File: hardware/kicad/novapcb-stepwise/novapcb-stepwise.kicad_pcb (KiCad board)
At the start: 6 copper layers, 90 x 70 mm, 129 parts, among them J1 USB-C_2.0, J10 CRSF_solder_pad, J11 ESC_solder_pad, J12 ESC_solder_pad, J13 ESC_solder_pad, J14 ESC_solder_pad, J15 ESC_solder_pad, J16 ESC_solder_pad, J17 ESC_solder_pad, J18 ESC_solder_pad, J19 MAUCH2_6P, J2 microSD_DM3AT, J20 CAN_4P, J3 TELEM_6P, J4 MAUCH_6P, J5 GPS_MAG_10P, J9 SWD_10P, Q2 AO3401A, Q3 AO4262E, Q4 AO4262E, Q5 AO3400A, U1 STM32H743VITx, U11 LM74700-Q1, U12 LM74700-Q1, U13 LP5907MFX-3.3, U14 TJA1051TK/3, U15 PESD2CAN, U2 AP2112K-3.3, U3 ICM-42688-P_LGA-14_2.5x3mm_P0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, U4 DPS310, U5 USBLC6-2P6, U6 TPS25940A, U7 LPS22HB, U8 BMI088, U9 LSM6DSV16X, Y1 8MHz

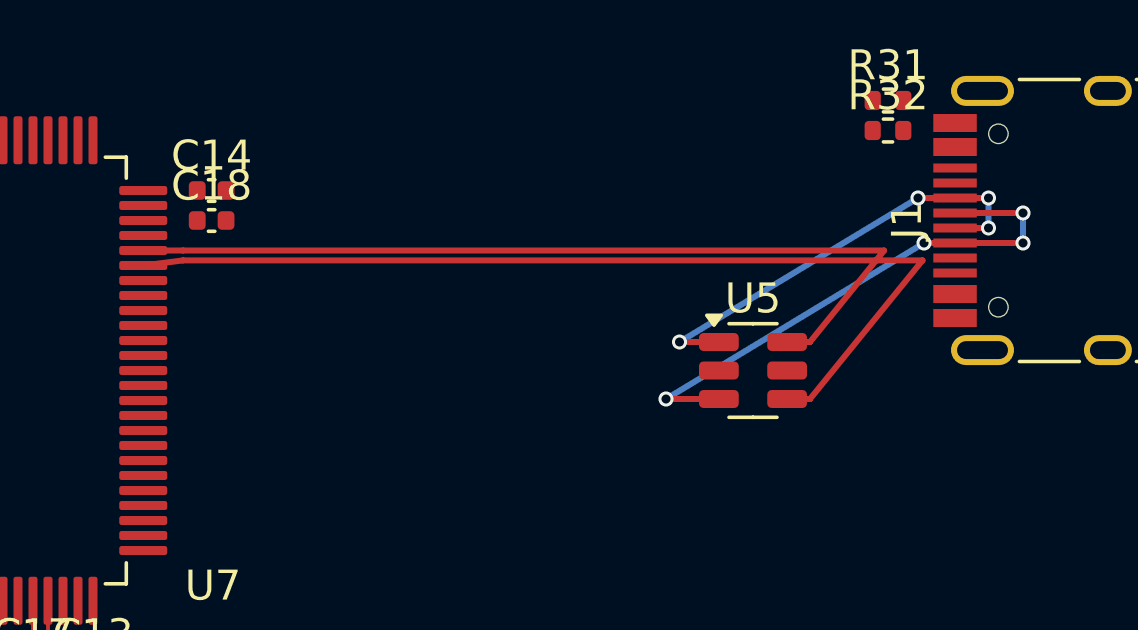
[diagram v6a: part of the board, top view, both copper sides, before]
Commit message: hw: C↔F route — wing topology attempt; geometric impasse documented
Per master 2026-05-23: confirmed pair order at U1 (DM south, DP north)
MATCHES U5 (DM south, DP north). NO topological crossover needed.

## Geometric finding (independent of pair-order)

The DM-DP violation is NOT a topological crossover. It's a
PERPENDICULAR-DISTANCE constraint:

  pair pitch S+W = 0.33mm
  diagonal at angle θ from horizontal
  perpendicular trace-trace distance = 0.33 * cos(θ)

For ≥0.10mm edge gap (USB_diffpair clearance):
  perp distance ≥ 0.30mm
  cos(θ) ≥ 0.909
  θ ≤ 24.6°

DM descent: 4.62mm Y over (X_M_H - X_FAN_END) X-span.
For θ ≤ 24.6°: X-span ≥ 10.1mm.
With X_FAN_END=74.90 (pin5 clearance): X_M_H ≥ 85.0mm.
But X_M_H ≤ 78.71mm (J1 A5 USBC_CC1 pad clearance).

NOT POSSIBLE with U5 at X=73.

## Tried topologies

1. Single straight diag, same-X start (X_M_H = X_P_H = 78.65): perp distance 0.21mm → edge 0.01mm — 5 violations
2. Stagger DP later (X_P_H < X_M_H): pair order flips in descent — crossing
3. Stagger DM later (X_M_H < X_P_H): DP descent crosses DM coupled-H Y=31.33 (X<X_M_H) — 1 violation persistent
4. Wing topology (vertical jog before diag to widen pair): DM wing south cap overlaps DP diag — 5 violations

All single-layer F.Cu approaches hit the perp-distance bound.

## Options

(C') Move U5 further west — analyzed:
  - For θ ≤ 40° (acceptable edge gap ~0.05mm): X-span ≥ 5.51mm → X_M_H ≥ 80.4mm. Still NOT possible.
  - For θ ≤ 30° (perp 0.286mm, edge 0.086mm): X-span ≥ 8.0mm → X_M_H ≥ 82.9. Not possible.
  - Need U5 X very west to provide X-span. U5 X = 67 gives X-span = X_M_H - U5_X - 1.90 = 78.71 - 68.90 = 9.81mm → θ = atan(4.62/9.81) = 25°. Marginal.
  - U5 at X=66 → X-span 10.81 → θ = 23° → perp 0.305mm → edge 0.105mm. CLEAR.

(B') B.Cu jog: introduces TOPOLOGICAL crossing of DP B.Cu with pre-ESD pair B.Cu. Pre-ESD requires re-route or also use B.Cu.

(A') Use wider pair pitch (S=0.20 instead of 0.13) for coupled section:
  - Pair pitch 0.40mm → perp at 51° =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
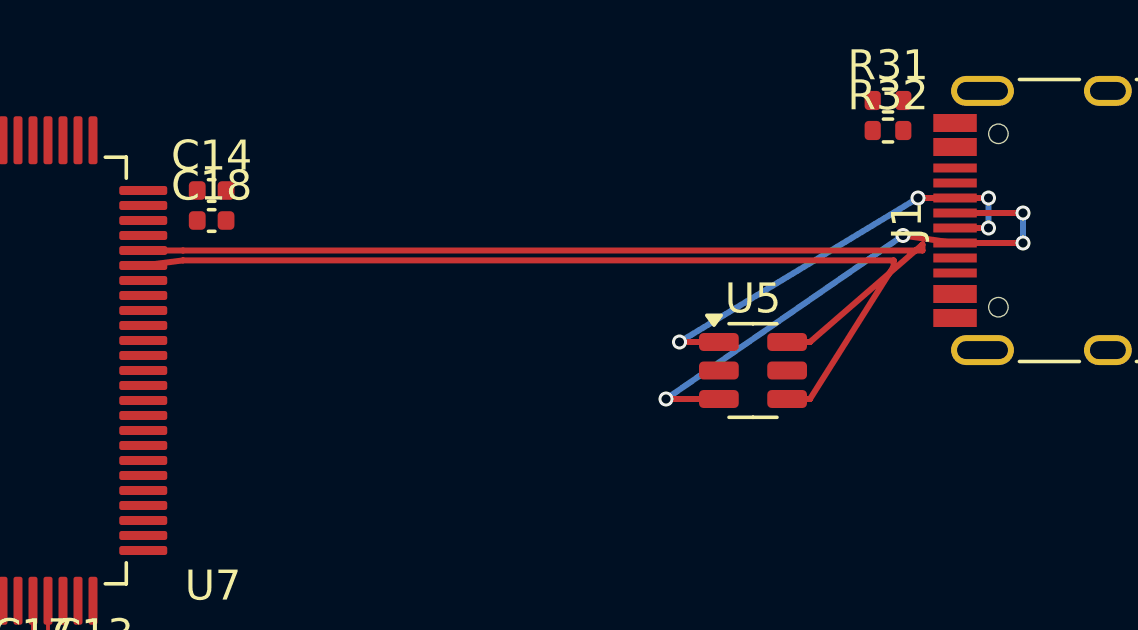
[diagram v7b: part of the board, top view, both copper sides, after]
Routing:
- net USB_DP: track 29.4 -> 31.9 mm
- net USB_DM: track 32.7 -> 31.2 mm
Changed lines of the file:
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@@
 	)
 	(segment
-		(start 78.7 30.75)
+		(start 78 30.5)
 		(end 79.735 30.75)
+		(width 0.2)
+		(layer "F.Cu")
+		(net 93)
+	)
+	(segment
+		(start 79.735 29.75)
+		(end 82 29.75)
+		(width 0.2)
+		(layer "F.Cu")
+		(net 93)
+	)
+	(segment
+		(start 71.8625 35.95)
+		(end 70.1 35.95)
 		(width 0.2)
 		(layer "F.Cu")
@@
 		(net 93)
 	)
-	(segment
-		(start 79.735 29.75)
-		(end 82 29.75)
-		(width 0.2)
-		(layer "F.Cu")
-		(net 93)
-	)
-	(segment
-		(start 71.8625 35.95)
-		(end 70.1 35.95)
-		(width 0.2)
-		(layer "F.Cu")
-		(net 93)
-	)
 	(via
 		(at 70.1 35.95)
@@
 	)
 	(via
+		(at 82 29.75)
+		(size 0.5)
+		(drill 0.3)
+		(layers "F.Cu" "B.Cu")
+		(net 93)
+	)
+	(via
+		(at 78 30.5)
+		(size 0.5)
+		(drill 0.3)
+		(layers "F.Cu" "B.Cu")
+		(net 93)
+	)
+	(via
 		(at 82 30.75)
 		(size 0.5)
 		(drill 0.3)
 		(layers "F.Cu" "B.Cu")
-		(net 93)
-	)
-	(via
-		(at 78.7 30.75)
-		(size 0.5)
-		(drill 0.3)
-		(layers "F.Cu" "B.Cu")
-		(net 93)
-	)
-	(via
-		(at 82 29.75)
-		(size 0.5)
-		(drill 0.3)
-		(layers "F.Cu" "B.Cu")
-		(net 93)
-	)
-	(segment
-		(start 70.1 35.95)
-		(end 78.7 30.75)
-		(width 0.2)
-		(layer "B.Cu")
 		(net 93)
 	)
@@
 	)
 	(segment
+		(start 70.1 35.95)
+		(end 78 30.5)
+		(width 0.2)
+		(layer "B.Cu")
+		(net 93)
+	)
+	(segment
+		(start 78.5 29.25)
+		(end 79.735 29.25)
+		(width 0.2)
+		(layer "F.Cu")
+		(net 94)
+	)
+	(segment
+		(start 80.85 29.25)
+		(end 79.735 29.25)
+		(width 0.2)
+		(layer "F.Cu")
+		(net 94)
+	)
+	(segment
+		(start 79.735 30.25)
+		(end 80.85 30.25)
+		(width 0.2)
+		(layer "F.Cu")
+		(net 94)
+	)
+	(segment
 		(start 71.8625 34.05)
 		(end 70.55 34.05)
@@
 		(net 94)
 	)
-	(segment
-		(start 80.85 29.25)
-		(end 79.735 29.25)
-		(width 0.2)
-		(layer "F.Cu")
-		(net 94)
-	)
-	(segment
-		(start 78.5 29.25)
-		(end 79.735 29.25)
-		(width 0.2)
-		(layer "F.Cu")
-		(net 94)
-	)
-	(segment
-		(start 79.735 30.25)
-		(end 80.85 30.25)
-		(width 0.2)
-		(layer "F.Cu")
-		(net 94)
-	)
 	(via
 		(at 70.55 34.05)
@@
 	)
 	(segment
-		(start 78.65 31.33)
+		(start 77.69 31.33)
+		(end 77.69 31.53)
+		(width 0.2)
+		(layer "F.Cu")
+		(net 95)
+	)
+	(segment
+		(start 77.69 31.53)
 		(end 74.9 35.95)
+		(width 0.2)
+		(layer "F.Cu")
+		(net 95)
+	)
+	(segment
+		(start 74.9 35.95)
+		(end 74.1375 35.95)
 		(width 0.2)
 		(layer "F.Cu")
@@
 	)
 	(segment
-		(start 74.9 35.95)
-		(end 74.1375 35.95)
-		(width 0.2)
-		(layer "F.Cu")
-		(net 95)
-	)
-	(segment
 		(start 54 31.33)
-		(end 78.65 31.33)
-		(width 0.2)
-		(layer "F.Cu")
-		(net 95)
+		(end 77.69 31.33)
+		(width 0.2)
+		(layer "F.Cu")
+		(net 95)
+	)
+	(segment
+		(start 78.65 30.8)
+		(end 74.9 34.05)
+		(width 0.2)
+		(layer "F.Cu")
+		(net 96)
+	)
+	(segment
+		(start 54 31)
+		(end 78.65 31)
+		(width 0.2)
+		(layer "F.Cu")
+		(net 96)
 	)
 	(segment
@@
 	)
 	(segment
-		(start 54 31)
-		(end 77.37 31)
+		(start 78.65 31)
+		(end 78.65 30.8)
 		(width 0.2)
 		(layer "F.Cu")
@@
 		(width 0.2)
 		(layer "F.Cu")
-		(net 96)
-	)
-	(segment
-		(start 77.37 31)
-		(end 74.9 34.05)
-		(width 0.2)
-		(layer "F.Cu")

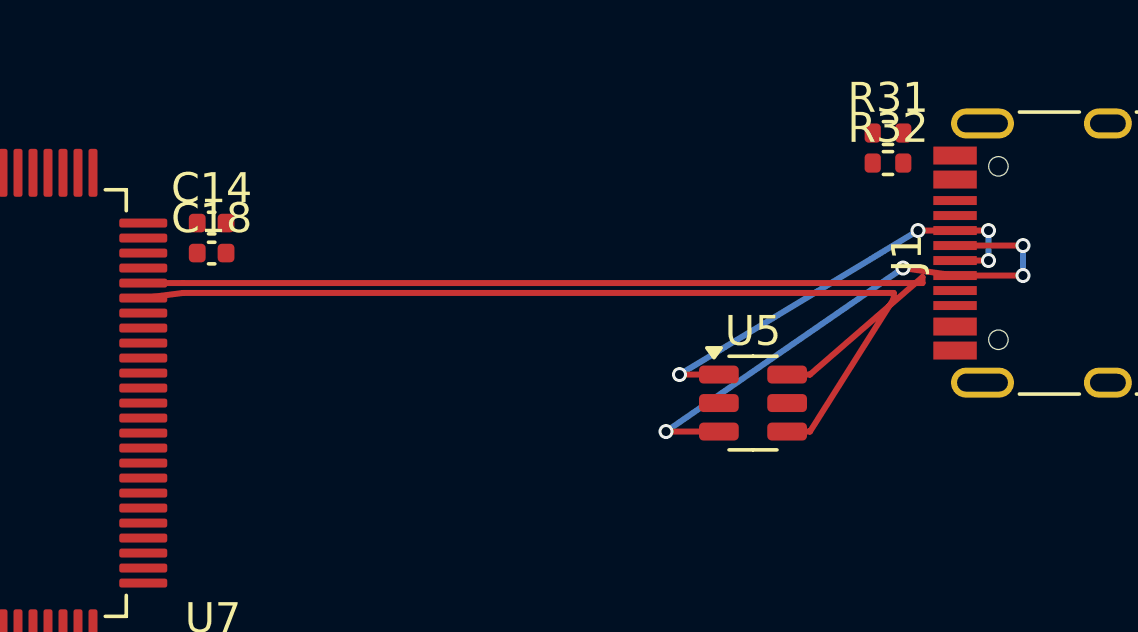
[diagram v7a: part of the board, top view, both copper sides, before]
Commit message: hw: U5 re-placed Y=31 (master root-cause); SOT-23-6 pin 2/3 block fan
Per master 2026-05-23 root-cause directive: U5 was at Y=35, forcing
4mm steep descent at 0.33mm coupled pitch (perp-distance failure).
Re-placed U5 at (73, 31) — pin 4 (DM, SE) and pin 6 (DP, NE)
straddle Y=31 corridor.

Trumpet fan from coupled Y=31.0/31.33 to pin 4 (Y=31.95) and
pin 6 (Y=30.05) — DM descent only 0.62mm, DP ascent only 0.95mm.
Much shallower than the 4.62mm DM descent at Y=35.

## SOT-23-6 inherent constraint discovered

But U5 pin 2 (GND, W mid, Y=31) and pin 5 (+5V, E mid, Y=31) sit
ON the pair Y=31 corridor. Worse, pin 3 (USBC_D_M_PRE, SW, Y=31.95)
sits where the DM fan needs to descend to pin 4 (also Y=31.95).

Pin 2 S edge (31.30) and pin 3 N edge (31.65) leave only 0.35mm
gap. Required channel for DM trace: 0.20mm trace + 2*0.20mm
clearance = 0.60mm. INSUFFICIENT.

Similarly pin 1 (USBC_D_P_PRE, NW, Y=30.05) blocks DP fan to
pin 6 (Y=30.05) — pin 1 Y range 29.75..30.35 overlaps DP target.

This is a SOT-23-6 inherent geometric issue: the side pins (1, 3
on west, 4, 6 on east) at Y_U5±0.95 are ONLY 1.9mm apart total,
which is the same scale as pair members + clearance. The corridor
pair (0.33mm pitch) cannot thread between pin 2 and pin 3 (gap
0.35mm) on F.Cu.

Trying various Y positions (Y=31, 31.4, 32) — all hit same issue
because pad sizes (1.325 × 0.6) and pin pitch (0.95) are similar
fixed dimensions.

Current state: 4 DRC violations (DM/DP coupled-H trace south edge
overlapping pin 2 GND in Y direction). Renders attached.

## Trying paths

This commit captures Y=31 placement + best routing attempt. Going
to ping master with SOT-23-6 pin geometry finding for direction
on:
- (a) B.Cu jog limited to U5 body region (master previously
      rejected as "unneeded once Y-aligned" — but Y-align reveals
      this SOT-23-6 side pin constraint)
- (b) Detour around U5 body (north or south) — long, breaks coupling
- (c) Slightly offset U5 Y (33-34) — recreates the steep descent

C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
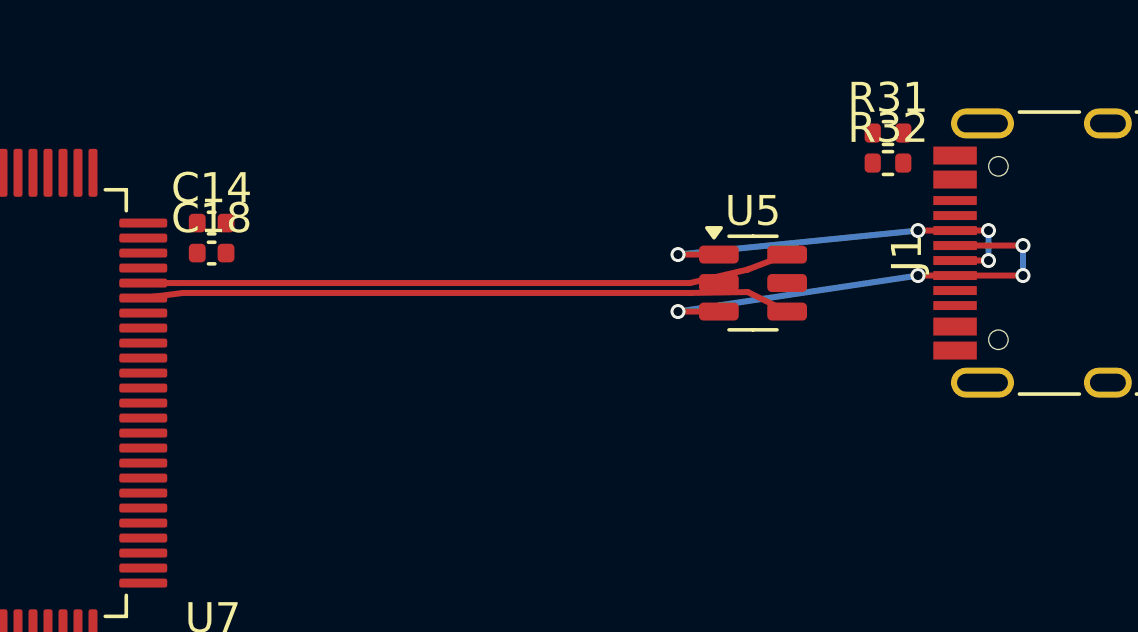
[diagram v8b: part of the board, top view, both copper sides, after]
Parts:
- moved U5 4.00 mm to (73.0, 31.0)
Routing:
- net USB_DP: track 31.9 -> 21.6 mm
- net USB_DM: track 31.2 -> 21.6 mm
- net USBC_D_M_PRE: track 18.6 -> 16.2 mm
- net USBC_D_P_PRE: track 15.1 -> 13.9 mm
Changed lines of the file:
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@@
 	(footprint "Package_TO_SOT_SMD:SOT-23-6"
 		(layer "F.Cu")
-		(at 73 35)
+		(at 73 31)
 		(descr "SOT, 6 Pin (JEDEC MO-178 Var AB https://www.jedec.org/document_search?search_api_views_fulltext=MO-178), generated with kicad-footprint-generator ipc_gullwing_generator.py")
 		(tags "SOT TO_SOT_SMD")
@@
 	)
 	(segment
-		(start 78 30.5)
-		(end 79.735 30.75)
-		(width 0.2)
-		(layer "F.Cu")
-		(net 93)
-	)
-	(segment
 		(start 79.735 29.75)
 		(end 82 29.75)
@@
 	)
 	(segment
-		(start 71.8625 35.95)
-		(end 70.1 35.95)
+		(start 78.5 30.75)
+		(end 79.735 30.75)
 		(width 0.2)
 		(layer "F.Cu")
@@
 		(net 93)
 	)
+	(segment
+		(start 71.8625 31.95)
+		(end 70.5 31.95)
+		(width 0.2)
+		(layer "F.Cu")
+		(net 93)
+	)
 	(via
-		(at 70.1 35.95)
+		(at 70.5 31.95)
+		(size 0.5)
+		(drill 0.3)
+		(layers "F.Cu" "B.Cu")
+		(net 93)
+	)
+	(via
+		(at 82 30.75)
 		(size 0.5)
 		(drill 0.3)
@@
 	)
 	(via
-		(at 78 30.5)
+		(at 78.5 30.75)
 		(size 0.5)
 		(drill 0.3)
@@
 		(net 93)
 	)
-	(via
-		(at 82 30.75)
-		(size 0.5)
-		(drill 0.3)
-		(layers "F.Cu" "B.Cu")
+	(segment
+		(start 70.5 31.95)
+		(end 78.5 30.75)
+		(width 0.2)
+		(layer "B.Cu")
 		(net 93)
 	)
@@
 	)
 	(segment
-		(start 70.1 35.95)
-		(end 78 30.5)
+		(start 79.735 30.25)
+		(end 80.85 30.25)
 		(width 0.2)
-		(layer "B.Cu")
-		(net 93)
+		(layer "F.Cu")
+		(net 94)
+	)
+	(segment
+		(start 71.8625 30.05)
+		(end 70.5 30.05)
+		(width 0.2)
+		(layer "F.Cu")
+		(net 94)
+	)
+	(segment
+		(start 80.85 29.25)
+		(end 79.735 29.25)
+		(width 0.2)
+		(layer "F.Cu")
+		(net 94)
 	)
 	(segment
@@
 		(net 94)
 	)
-	(segment
-		(start 80.85 29.25)
-		(end 79.735 29.25)
-		(width 0.2)
-		(layer "F.Cu")
+	(via
+		(at 70.5 30.05)
+		(size 0.5)
+		(drill 0.3)
+		(layers "F.Cu" "B.Cu")
 		(net 94)
 	)
-	(segment
-		(start 79.735 30.25)
-		(end 80.85 30.25)
-		(width 0.2)
-		(layer "F.Cu")
-		(net 94)
-	)
-	(segment
-		(start 71.8625 34.05)
-		(end 70.55 34.05)
-		(width 0.2)
-		(layer "F.Cu")
-		(net 94)
-	)
 	(via
-		(at 70.55 34.05)
+		(at 80.85 30.25)
 		(size 0.5)
 		(drill 0.3)
@@
 		(net 94)
 	)
-	(via
-		(at 80.85 30.25)
-		(size 0.5)
-		(drill 0.3)
-		(layers "F.Cu" "B.Cu")
-		(net 94)
-	)
 	(segment
 		(start 80.85 30.25)
@@
 	)
 	(segment
-		(start 70.55 34.05)
+		(start 70.5 30.05)
 		(end 78.5 29.25)
 		(width 0.2)
@@
 	)
 	(segment
-		(start 77.69 31.33)
-		(end 77.69 31.53)
+		(start 72.825 31.3)
+		(end 74.138 31.95)
 		(width 0.2)
 		(layer "F.Cu")
@@
 	)
 	(segment
-		(start 77.69 31.53)
-		(end 74.9 35.95)
-		(width 0.2)
-		(layer "F.Cu")
-		(net 95)
-	)
-	(segment
-		(start 74.9 35.95)
-		(end 74.1375 35.95)
+		(start 54 31.33)
+		(end 70.9 31.33)
 		(width 0.2)
 		(layer "F.Cu")
@@
 	)
 	(segment
-		(start 54 31.33)
-		(end 77.69 31.33)
+		(start 70.9 31.33)
+		(end 72.825 31.3)
 		(width 0.2)
 		(layer "F.Cu")
@@
 	)
 	(segment
-		(start 78.65 30.8)
-		(end 74.9 34.05)
+		(start 72.825 30.55)
+		(end 74.138 30.05)
 		(width 0.2)
 		(layer "F.Cu")
@@
 	(segment
 		(start 54 31)
-		(end 78.65 31)
+		(end 70.9 31)
 		(width 0.2)
 		(layer "F.Cu")
@@
 	)
 	(segment
-		(start 74.9 34.05)
-		(end 74.1375 34.05)
+		(start 70.9 31)
+		(end 72.825 30.55)
 		(width 0.2)
 		(layer "F.Cu")
-		(net 96)
-	)
-	(segment
-		(start 78.65 31)
-		(end 78.65 30.8)
-		(width 0.2)
-		(layer "F.Cu")
